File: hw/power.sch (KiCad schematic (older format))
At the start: 19 parts, among them J4 POWER, U10 MCP1826S, U9 MCP16301H

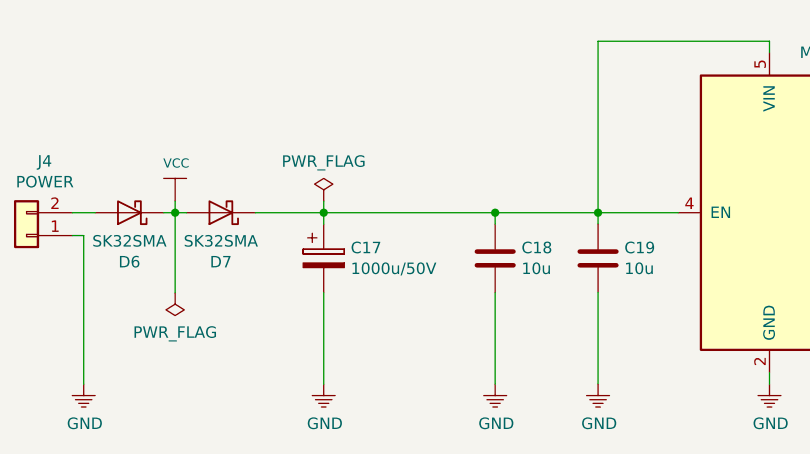
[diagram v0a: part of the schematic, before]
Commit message: assigned footprints
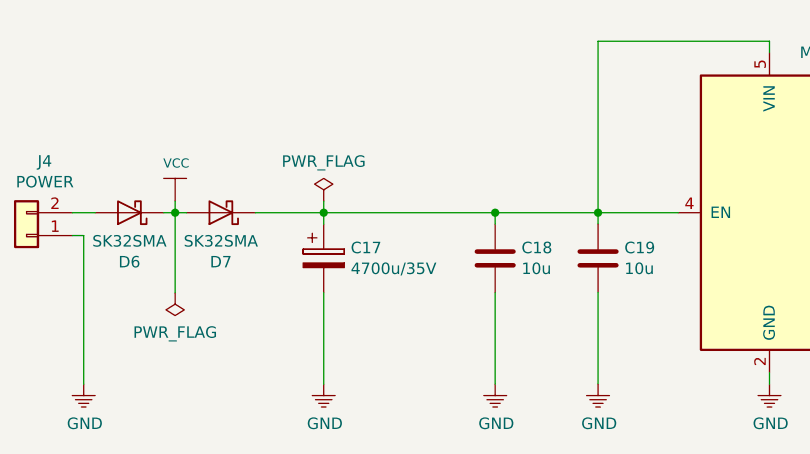
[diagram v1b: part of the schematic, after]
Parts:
- C17: value 1000u/50V -> 4700u/35V; footprint (none) -> Capacitors_THT:CP_Radial_D18.0mm_P7.50mm
- C18, C19: footprint (none) -> Capacitors_SMD:C_2220_HandSoldering
- C20, C21, C22, C23, C24, C25: footprint (none) -> Capacitors_SMD:C_0805_HandSoldering
- D6, D7, D8, D9: footprint (none) -> Diodes_SMD:D_SMA
- J4: footprint (none) -> Socket_Strips:Socket_Strip_Straight_1x02_Pitch2.54mm
- L1: footprint (none) -> Choke_SMD:Choke_SMD_7.3x7.3_H4.5
- R18, R19: footprint (none) -> Resistors_SMD:R_0805_HandSoldering
- U10: footprint (none) -> TO_SOT_Packages_SMD:SOT-223-3Lead_TabPin2
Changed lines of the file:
@@
 F 0 "J4" H 1670 3625 50  0000 C CNN
 F 1 "POWER" H 1670 3716 50  0000 C CNN
-F 2 "" H 1750 3950 50  0001 C CNN
+F 2 "Socket_Strips:Socket_Strip_Straight_1x02_Pitch2.54mm" H 1750 3950 50  0001 C CNN
 F 3 "~" H 1750 3950 50  0001 C CNN
 	1    1750 3950
@@
 P 3050 4050
 F 0 "C17" H 3168 4096 50  0000 L CNN
-F 1 "1000u/50V" H 3168 4005 50  0000 L CNN
-F 2 "" H 3088 3900 50  0001 C CNN
+F 1 "4700u/35V" H 3168 4005 50  0000 L CNN
+F 2 "Capacitors_THT:CP_Radial_D18.0mm_P7.50mm" H 3088 3900 50  0001 C CNN
 F 3 "" H 3050 4050 50  0001 C CNN
 	1    3050 4050
@@
 F 0 "C20" H 5815 3696 50  0000 L CNN
 F 1 "100n" H 5815 3605 50  0000 L CNN
-F 2 "" H 5738 3500 50  0001 C CNN
+F 2 "Capacitors_SMD:C_0805_HandSoldering" H 5738 3500 50  0001 C CNN
 F 3 "" H 5700 3650 50  0001 C CNN
 	1    5700 3650
@@
 F 0 "D8" V 5654 4129 50  0000 L CNN
 F 1 "SK32SMA" V 5745 4129 50  0000 L CNN
-F 2 "" H 5700 4050 50  0001 C CNN
+F 2 "Diodes_SMD:D_SMA" H 5700 4050 50  0001 C CNN
 F 3 "" H 5700 4050 50  0001 C CNN
 	1    5700 4050
@@
 F 0 "D9" H 6350 3666 50  0000 C CNN
 F 1 "SK32SMA" H 6350 3575 50  0000 C CNN
-F 2 "" H 6350 3450 50  0001 C CNN
+F 2 "Diodes_SMD:D_SMA" H 6350 3450 50  0001 C CNN
 F 3 "" H 6350 3450 50  0001 C CNN
 	1    6350 3450
@@
 F 0 "L1" V 6540 3850 50  0000 C CNN
 F 1 "DE0704-22" V 6449 3850 50  0000 C CNN
-F 2 "" H 6350 3850 50  0001 C CNN
+F 2 "Choke_SMD:Choke_SMD_7.3x7.3_H4.5" H 6350 3850 50  0001 C CNN
 F 3 "" H 6350 3850 50  0001 C CNN
 	1    6350 3850
@@
 F 0 "C21" H 6865 4096 50  0000 L CNN
 F 1 "10u" H 6865 4005 50  0000 L CNN
-F 2 "" H 6788 3900 50  0001 C CNN
+F 2 "Capacitors_SMD:C_0805_HandSoldering" H 6788 3900 50  0001 C CNN
 F 3 "" H 6750 4050 50  0001 C CNN
 	1    6750 4050
@@
 F 0 "C22" H 7215 4096 50  0000 L CNN
 F 1 "10u" H 7215 4005 50  0000 L CNN
-F 2 "" H 7138 3900 50  0001 C CNN
+F 2 "Capacitors_SMD:C_0805_HandSoldering" H 7138 3900 50  0001 C CNN
 F 3 "" H 7100 4050 50  0001 C CNN
 	1    7100 4050
@@
 F 0 "R18" H 7520 4096 50  0000 L CNN
 F 1 "330k" H 7520 4005 50  0000 L CNN
-F 2 "" V 7380 4050 50  0001 C CNN
+F 2 "Resistors_SMD:R_0805_HandSoldering" V 7380 4050 50  0001 C CNN
 F 3 "" H 7450 4050 50  0001 C CNN
 	1    7450 4050
@@
 F 0 "R19" H 7520 4496 50  0000 L CNN
 F 1 "56k" H 7520 4405 50  0000 L CNN
-F 2 "" V 7380 4450 50  0001 C CNN
+F 2 "Resistors_SMD:R_0805_HandSoldering" V 7380 4450 50  0001 C CNN
 F 3 "" H 7450 4450 50  0001 C CNN
 	1    7450 4450
@@
 F 0 "C19" H 4365 4096 50  0000 L CNN
 F 1 "10u" H 4365 4005 50  0000 L CNN
-F 2 "" H 4288 3900 50  0001 C CNN
+F 2 "Capacitors_SMD:C_2220_HandSoldering" H 4288 3900 50  0001 C CNN
 F 3 "" H 4250 4050 50  0001 C CNN
 	1    4250 4050
@@
 F 0 "C18" H 3915 4096 50  0000 L CNN
 F 1 "10u" H 3915 4005 50  0000 L CNN
-F 2 "" H 3838 3900 50  0001 C CNN
+F 2 "Capacitors_SMD:C_2220_HandSoldering" H 3838 3900 50  0001 C CNN
 F 3 "" H 3800 4050 50  0001 C CNN
 	1    3800 4050
@@
 F 0 "U10" H 8400 4092 50  0000 C CNN
 F 1 "MCP1826S" H 8400 4001 50  0000 C CNN
-F 2 "" H 8300 4000 50  0001 C CNN
+F 2 "TO_SOT_Packages_SMD:SOT-223-3Lead_TabPin2" H 8300 4000 50  0001 C CNN
 F 3 "http://ww1.microchip.com/downloads/en/DeviceDoc/22057B.pdf" H 8400 4100 50  0001 C CNN
 	1    8400 3850
@@
 F 0 "C23" H 7965 4096 50  0000 L CNN
 F 1 "100n" H 7965 4005 50  0000 L CNN
-F 2 "" H 7888 3900 50  0001 C CNN
+F 2 "Capacitors_SMD:C_0805_HandSoldering" H 7888 3900 50  0001 C CNN
 F 3 "" H 7850 4050 50  0001 C CNN
 	1    7850 4050
@@
 F 0 "C24" H 8865 4096 50  0000 L CNN
 F 1 "100n" H 8865 4005 50  0000 L CNN
-F 2 "" H 8788 3900 50  0001 C CNN
+F 2 "Capacitors_SMD:C_0805_HandSoldering" H 8788 3900 50  0001 C CNN
 F 3 "" H 8750 4050 50  0001 C CNN
 	1    8750 4050
@@
 F 0 "C25" H 9368 4096 50  0000 L CNN
 F 1 "10u" H 9368 4005 50  0000 L CNN
-F 2 "" H 9288 3900 50  0001 C CNN
+F 2 "Capacitors_SMD:C_0805_HandSoldering" H 9288 3900 50  0001 C CNN
 F 3 "" H 9250 4050 50  0001 C CNN
 	1    9250 4050
@@
 $EndComp
 $Comp
-L PWR_FLAG #FLG02
+L PWR_FLAG #FLG03
 U 1 1 59FB138C
 P 7100 3800
-F 0 "#FLG02" H 7100 3875 50  0001 C CNN
+F 0 "#FLG03" H 7100 3875 50  0001 C CNN
 F 1 "PWR_FLAG" H 7100 3974 50  0000 C CNN
 F 2 "" H 7100 3800 50  0001 C CNN
@@
 F 0 "D7" H 2600 4066 50  0000 C CNN
 F 1 "SK32SMA" H 2600 3975 50  0000 C CNN
-F 2 "" H 2600 3850 50  0001 C CNN
+F 2 "Diodes_SMD:D_SMA" H 2600 3850 50  0001 C CNN
 F 3 "" H 2600 3850 50  0001 C CNN
 	1    2600 3850
@@
 F 0 "D6" H 2200 4066 50  0000 C CNN
 F 1 "SK32SMA" H 2200 3975 50  0000 C CNN
-F 2 "" H 2200 3850 50  0001 C CNN
+F 2 "Diodes_SMD:D_SMA" H 2200 3850 50  0001 C CNN
 F 3 "" H 2200 3850 50  0001 C CNN
 	1    2200 3850
@@
 Connection ~ 2400 3850
 $Comp
-L PWR_FLAG #FLG03
+L PWR_FLAG #FLG02
 U 1 1 5A031640
 P 3050 3800
-F 0 "#FLG03" H 3050 3875 50  0001 C CNN
+F 0 "#FLG02" H 3050 3875 50  0001 C CNN
 F 1 "PWR_FLAG" H 3050 3974 50  0000 C CNN
 F 2 "" H 3050 3800 50  0001 C CNN

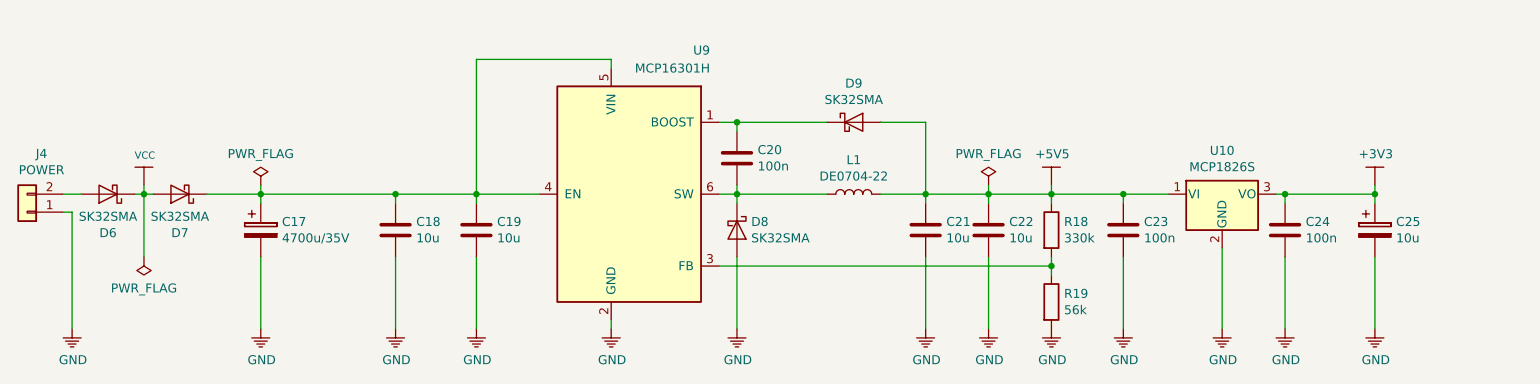
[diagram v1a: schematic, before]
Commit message: reduced schematic
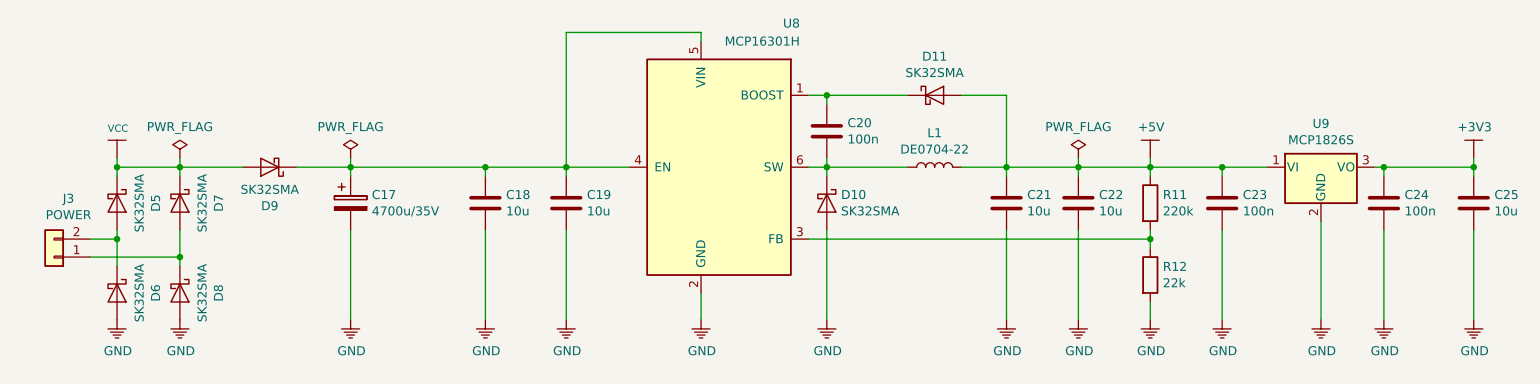
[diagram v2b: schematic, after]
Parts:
- removed C25: 10u, Capacitors_SMD:C_0805_HandSoldering, symbol CP
- added C25: 10u, Capacitors_SMD:C_0805_HandSoldering, symbol C
- added D6, D7, D8: SK32SMA, Diodes_SMD:D_SMA, symbol D_Schottky
- C17: footprint Capacitors_THT:CP_Radial_D18.0mm_P7.50mm -> Capacitors_THT:CP_Radial_D4.0mm_P1.50mm
- J3: renamed from J4; footprint Socket_Strips:Socket_Strip_Straight_1x02_Pitch2.54mm -> Pin_Headers:Pin_Header_Straight_1x02_Pitch2.54mm
- R11: renamed from R18; value 330k -> 220k
- R12: renamed from R19; value 56k -> 22k
- renumbered D8 to D10, D9 to D11, D6 to D5, D7 to D9, U9 to U8, U10 to U9
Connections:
- net +3V3: now also C25.1
- net GND: now also C25.2, D6.2 (A), D8.2 (A); no longer J3.1 (Pin_1)
- net VCC: now also D7.1 (K)
- net at D5.2 (A), J3.2 (Pin_2): now also D6.1 (K)
- net +5V5 renamed +5V
- new net: D7.2 (A), D8.1 (K), J3.1 (Pin_1)
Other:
- moved on the sheet: C17, C18, C19, C20, C21, C22, C23, C24, D10, D11, D5, D9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
